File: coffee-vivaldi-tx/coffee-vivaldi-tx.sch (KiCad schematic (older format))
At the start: 40 parts, among them U1 MAX2750AUA+, U2 SE2565T-R, U3 SMA_PCB_Edge_Mount, U4 SMA_PCB_Edge_Mount

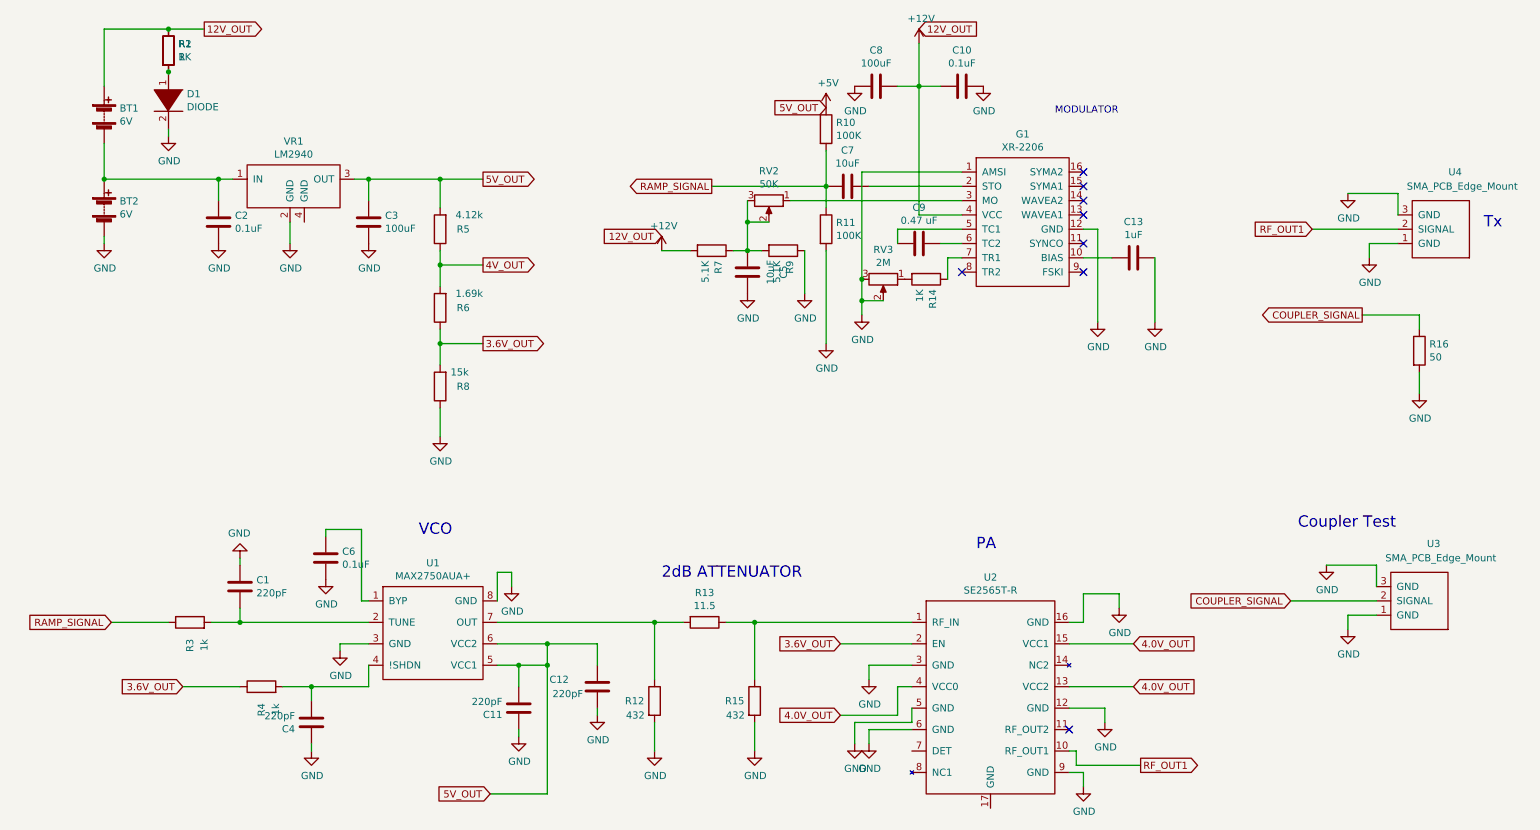
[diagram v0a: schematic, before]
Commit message: Coffee can radar tx update
Finalized schematic and initial PCB design.
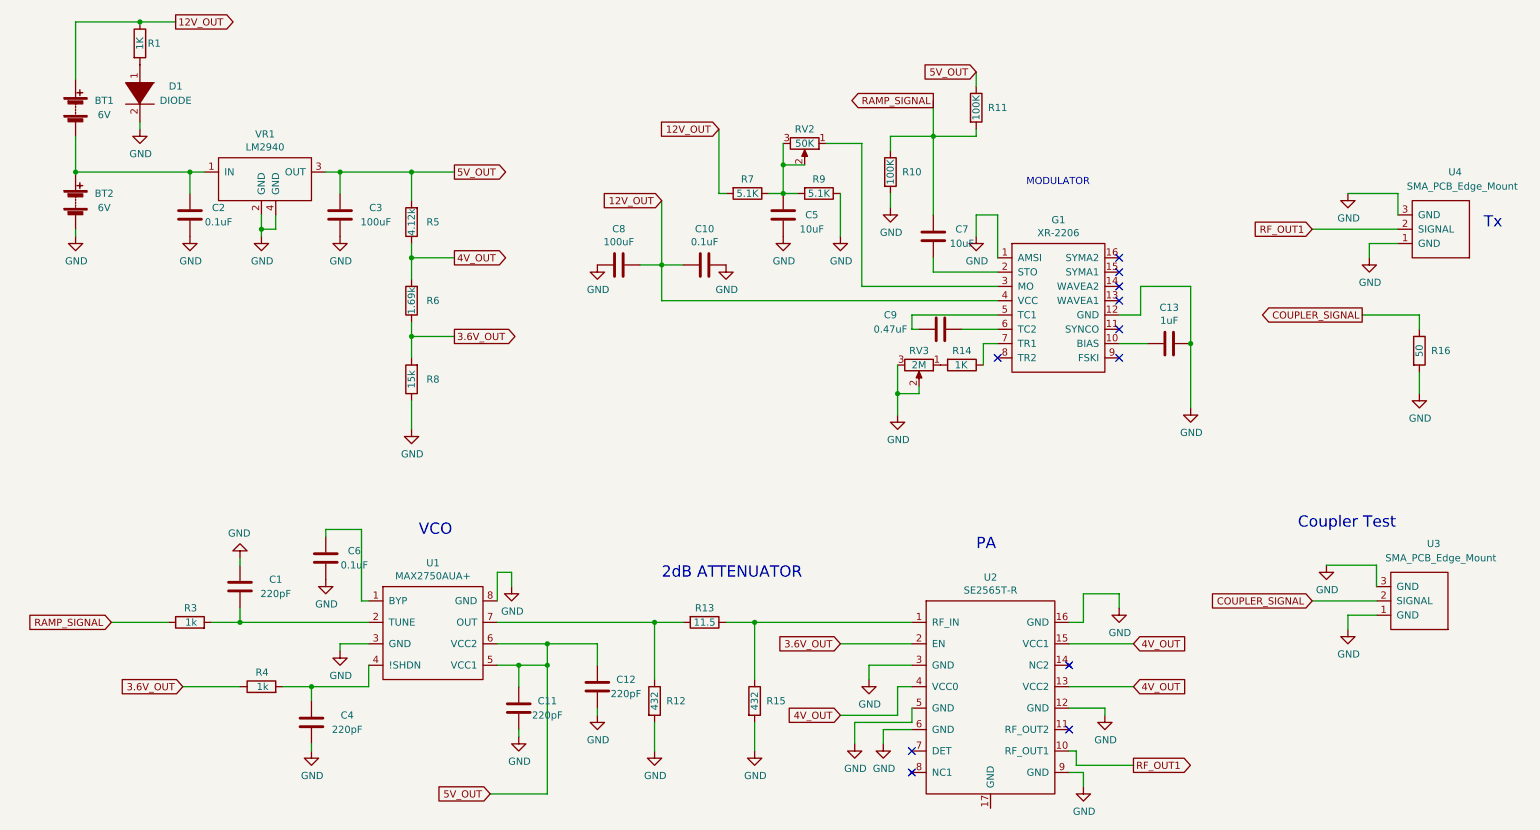
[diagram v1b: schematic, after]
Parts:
- removed R2: R, symbol Device:R
- BT1, BT2: footprint (none) -> Connector_PinSocket_2.54mm:PinSocket_1x02_P2.54mm_Vertical
- C1, C10, C11, C12, C13, C2, C3, C4, C5, C6, C7, C8: footprint (none) -> Capacitor_SMD:C_0805_2012Metric
- C9: value 0.47 uF -> 0.47uF; footprint (none) -> Capacitor_SMD:C_0805_2012Metric
- D1: footprint (none) -> LED_THT:LED_D5.0mm
- G1: footprint (none) -> HS2-PARTS:XR-2206
- R1, R10, R11, R12, R13, R14, R15, R16, R3, R4, R5, R6, R7, R8, R9: footprint (none) -> Resistor_SMD:R_0805_2012Metric
- RV2, RV3: footprint (none) -> HS2-PARTS:PV36W
- U1: footprint (none) -> HS2-PARTS:MAX2750AUA+
- U2: footprint (none) -> HS2-PARTS:SE2565T-R
- U3, U4: footprint (none) -> HS2-PARTS:SMA_EDGE_MOUNT_132255
- VR1: footprint (none) -> HS2-PARTS:LM2940
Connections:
- net +12V is gone; now on net 12V_OUT: C10.2, C8.1, G1.4 (VCC), R7.2
- net 4.0V_OUT is gone; now on net 4V_OUT: U2.13 (VCC2), U2.15 (VCC1), U2.4 (VCC0)
- net GND: now also R10.2, VR1.4 (GND); no longer R11.2
- net RAMP_SIGNAL: now also C7.1, R10.1, R11.2; no longer C7.2, R10.2, R11.1
- net at G1.2 (STO): now also C7.2; no longer C7.1
- net +5V renamed 5V_OUT
- net 5V_OUT: now also R11.1; no longer R10.1
- no-connect marks 8 -> 11
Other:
- moved on the sheet: BT1, BT2, C10, C13, C2, C3, C5, C7, C8, C9, D1, G1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

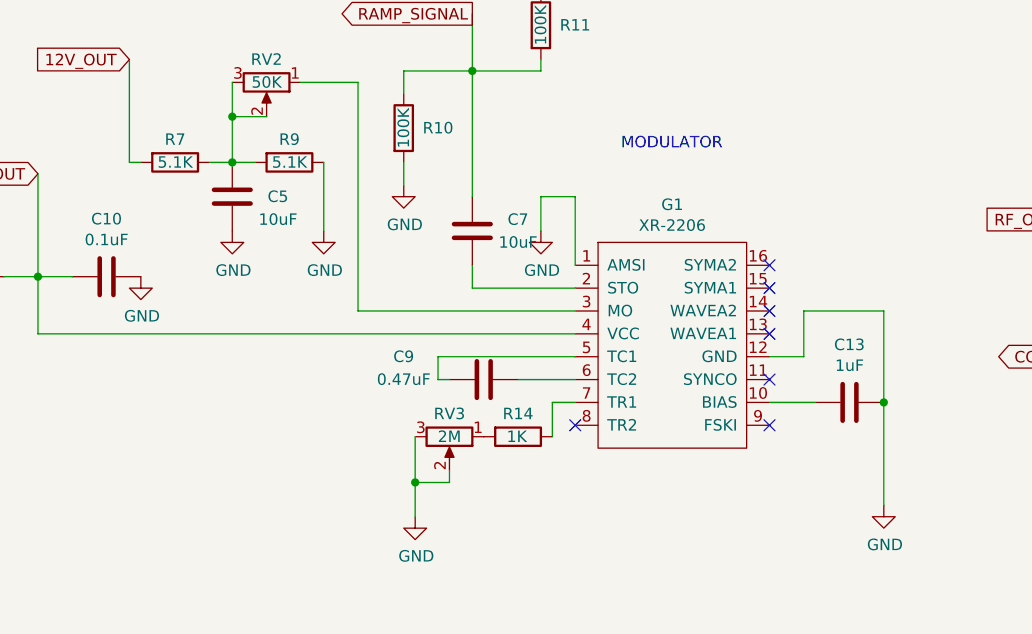
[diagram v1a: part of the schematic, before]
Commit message: Tx test board version 1
Components chosen, board ready for review
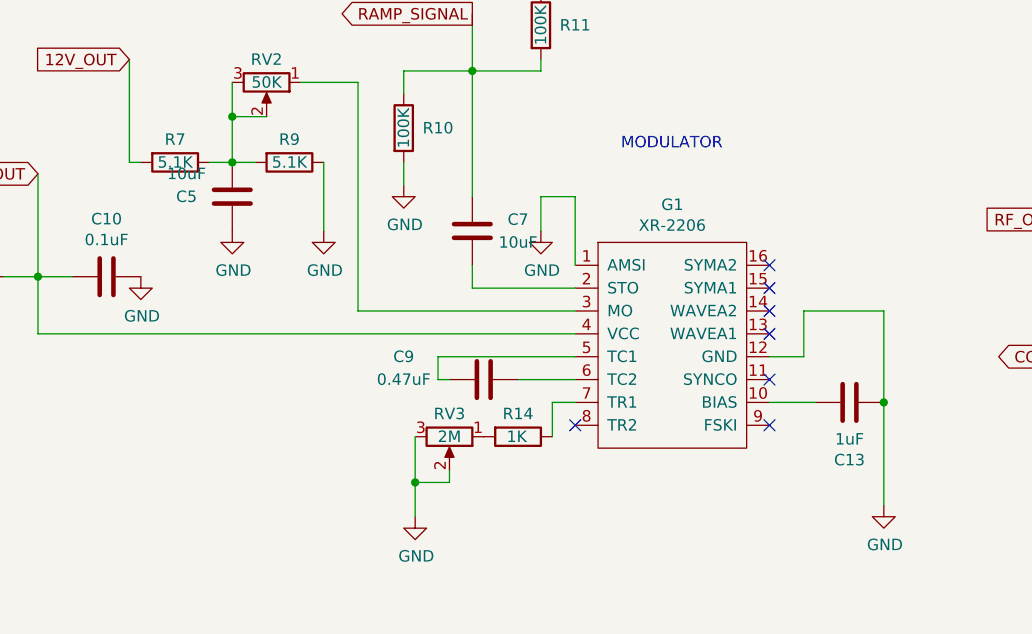
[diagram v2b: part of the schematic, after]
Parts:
- C13: footprint Capacitor_SMD:C_0805_2012Metric -> Capacitor_THT:CP_Radial_D4.0mm_P2.00mm
- C5, C7: footprint Capacitor_SMD:C_0805_2012Metric -> Capacitor_THT:CP_Radial_D5.0mm_P2.50mm
- C8: footprint Capacitor_SMD:C_0805_2012Metric -> Capacitor_THT:CP_Radial_D6.3mm_P2.50mm
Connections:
- net GND: now also C13.2, C5.2; no longer C13.1, C5.1
- net at G1.10 (BIAS): now also C13.1; no longer C13.2
- net at R7.1, R9.2, RV2.2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: now also C5.1; no longer C5.2
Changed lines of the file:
@@
 F 0 "C5" H 5650 2200 50  0000 C CNN
 F 1 "10uF" H 5650 2300 50  0000 C CNN
-F 2 "Capacitor_SMD:C_0805_2012Metric" H 5888 2050 50  0001 C CNN
+F 2 "Capacitor_THT:CP_Radial_D5.0mm_P2.50mm" H 5888 2050 50  0001 C CNN
 F 3 "~" H 5850 2200 50  0001 C CNN
 	1    5850 2200
-	-1   0    0    1
+	1    0    0    -1
 $EndComp
 Connection ~ 5850 2050
@@
 F 0 "C8" V 4448 2550 50  0000 C CNN
 F 1 "100uF" V 4539 2550 50  0000 C CNN
-F 2 "Capacitor_SMD:C_0805_2012Metric" H 4738 2400 50  0001 C CNN
+F 2 "Capacitor_THT:CP_Radial_D6.3mm_P2.50mm" H 4738 2400 50  0001 C CNN
 F 3 "~" H 4700 2550 50  0001 C CNN
 	1    4700 2550
@@
 F 0 "C13" V 8298 3100 50  0000 C CNN
 F 1 "1uF" V 8389 3100 50  0000 C CNN
-F 2 "Capacitor_SMD:C_0805_2012Metric" H 8588 2950 50  0001 C CNN
+F 2 "Capacitor_THT:CP_Radial_D4.0mm_P2.00mm" H 8588 2950 50  0001 C CNN
 F 3 "~" H 8550 3100 50  0001 C CNN
 	1    8550 3100
-	0    1    1    0
+	0    -1   -1   0
 $EndComp
 $Comp
@@
 F 0 "C7" H 7100 2400 50  0000 C CNN
 F 1 "10uF" H 7100 2300 50  0000 C CNN
-F 2 "Capacitor_SMD:C_0805_2012Metric" H 6938 2200 50  0001 C CNN
+F 2 "Capacitor_THT:CP_Radial_D5.0mm_P2.50mm" H 6938 2200 50  0001 C CNN
 F 3 "~" H 6900 2350 50  0001 C CNN
 	1    6900 2350

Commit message: Edited PCB dimensions, added gerber files
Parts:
- removed R8: 15k, Resistor_SMD:R_0805_2012Metric, symbol Device:R
- C13, C5, C8: symbol Device:C -> Device:CP
- R5: value 4.12k -> 3.83K
- R6: value 1.69k -> 10K
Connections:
- net 4V_OUT is gone; now on net 3.6V_OUT: R5.1, R6.2, U2.13 (VCC2), U2.15 (VCC1), U2.4 (VCC0)
- net 3.6V_OUT: no longer R6.1
- net GND: now also R6.1, U2.17 (GND)
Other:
- moved on the sheet: C1, C11, C12, C4, C6, R12, R13, R15, R3, R4, U1, U2

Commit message: Update schematic and PCB layout
reference for full design
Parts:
- C3: footprint Capacitor_SMD:C_0805_2012Metric -> Capacitor_THT:CP_Radial_D6.3mm_P2.50mm; symbol Device:C -> Device:CP
- R16: value 50 -> 51
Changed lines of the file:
@@
 $EndComp
 $Comp
-L Device:C C3
+L Device:CP C3
 U 1 1 6045E0D3
 P 2750 2200
 F 0 "C3" H 3000 2250 50  0000 C CNN
 F 1 "100uF" H 3000 2150 50  0000 C CNN
-F 2 "Capacitor_SMD:C_0805_2012Metric" H 2788 2050 50  0001 C CNN
+F 2 "Capacitor_THT:CP_Radial_D6.3mm_P2.50mm" H 2788 2050 50  0001 C CNN
 F 3 "~" H 2750 2200 50  0001 C CNN
 	1    2750 2200
@@
 P 10300 3150
 F 0 "R16" H 10450 3150 50  0000 C CNN
-F 1 "50" V 10300 3150 50  0000 C CNN
+F 1 "51" V 10300 3150 50  0000 C CNN
 F 2 "Resistor_SMD:R_0805_2012Metric" V 10230 3150 50  0001 C CNN
 F 3 "~" H 10300 3150 50  0001 C CNN
